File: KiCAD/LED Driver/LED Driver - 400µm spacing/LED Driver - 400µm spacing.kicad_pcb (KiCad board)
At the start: 2 copper layers, 13.1 x 9 mm, 6 parts, among them J1 0525590870, U1 LP5868TRKPR

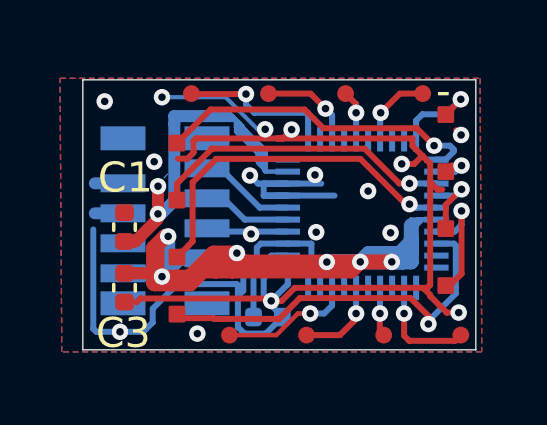
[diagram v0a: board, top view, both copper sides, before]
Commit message: Add controller - move ground
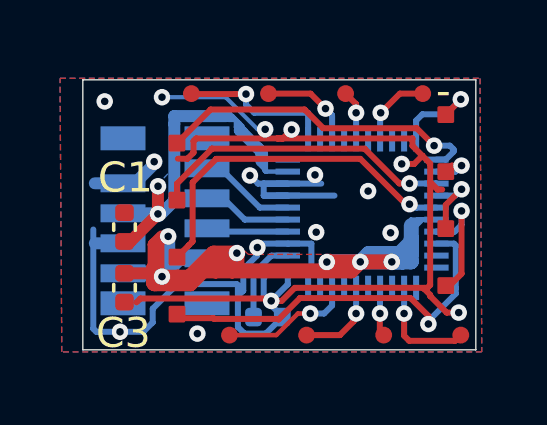
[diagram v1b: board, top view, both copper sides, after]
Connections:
- J1 pad 4: GND -> +5V
- J1 pad 6: +5V -> GND
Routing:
- net /VLED: track 41.4 -> 38.4 mm
- net GND: track 61.6 -> 62.8 mm, vias 17 -> 16
- net +5V: track 18.4 -> 17.5 mm
- added copper zone on F.Cu, net /VLED
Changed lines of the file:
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@@
 	(net 36 "unconnected-(U1-CS3-Pad4)")
 	(net 37 "unconnected-(U1-CS7-Pad8)")
+	(net 38 "unconnected-(J1-Pin_9-Pad9)")
+	(net 39 "unconnected-(J1-Pin_9-Pad9)_1")
+	(net 40 "unconnected-(J1-Pin_9-Pad9)_3")
 	(footprint "Capacitor_SMD:C_0402_1005Metric"
 		(layer "F.Cu")
@@
 			(size 0.6 1.5)
 			(layers "B.Cu" "B.Paste" "B.Mask")
-			(net 2 "GND")
+			(net 1 "+5V")
 			(pinfunction "Pin_4")
 			(pintype "passive")
@@
 			(size 0.6 1.5)
 			(layers "B.Cu" "B.Paste" "B.Mask")
-			(net 1 "+5V")
+			(net 2 "GND")
 			(pinfunction "Pin_6")
 			(pintype "passive")
@@
 			(size 0.8 1.5)
 			(layers "B.Cu" "B.Paste" "B.Mask")
-			(net 5 "unconnected-(J1-Pin_9-Pad9)_2")
+			(net 40 "unconnected-(J1-Pin_9-Pad9)_3")
 			(pinfunction "Pin_9")
 			(pintype "passive+no_connect")
@@
 			(size 0.8 1.5)
 			(layers "B.Cu" "B.Paste" "B.Mask")
-			(net 5 "unconnected-(J1-Pin_9-Pad9)_2")
+			(net 38 "unconnected-(J1-Pin_9-Pad9)")
 			(pinfunction "Pin_9")
 			(pintype "passive+no_connect")
@@
 			(size 0.8 1.5)
 			(layers "B.Cu" "B.Paste" "B.Mask")
-			(net 5 "unconnected-(J1-Pin_9-Pad9)_2")
+			(net 39 "unconnected-(J1-Pin_9-Pad9)_1")
 			(pinfunction "Pin_9")
 			(pintype "passive+no_connect")
@@
 	)
 	(segment
-		(start 47.88 35.09)
+		(start 47.715002 35.09)
 		(end 47.52 35.09)
 		(width 0.4)
@@
 	)
 	(segment
-		(start 48.635002 34.334998)
-		(end 47.88 35.09)
+		(start 48.635002 34.17)
+		(end 47.715002 35.09)
 		(width 0.4)
 		(layer "F.Cu")
@@
 	)
 	(segment
-		(start 48.655002 34.415002)
-		(end 49.28 33.790004)
-		(width 0.15)
+		(start 47.47 34.150004)
+		(end 48.615006 34.150004)
+		(width 0.4)
 		(layer "B.Cu")
 		(net 1)
@@
 	)
 	(segment
-		(start 47.92 35.150004)
-		(end 48.655002 34.415002)
-		(width 0.15)
-		(layer "B.Cu")
-		(net 1)
-	)
-	(segment
 		(start 51.370258 31.38)
 		(end 51.33 31.38)
@@
 	)
 	(segment
-		(start 48.655002 34.415002)
-		(end 48.635002 34.395002)
-		(width 0.15)
-		(layer "B.Cu")
-		(net 1)
-	)
-	(segment
-		(start 48.635002 34.395002)
-		(end 48.635002 34.17)
-		(width 0.15)
-		(layer "B.Cu")
-		(net 1)
-	)
-	(segment
-		(start 47.47 35.150004)
-		(end 47.92 35.150004)
-		(width 0.15)
-		(layer "B.Cu")
-		(net 1)
-	)
-	(segment
 		(start 51.98 31.989742)
 		(end 52.08 32.089742)
@@
 	)
 	(segment
+		(start 47.02 34.150004)
+		(end 47.47 34.150004)
+		(width 0.2)
+		(layer "B.Cu")
+		(net 1)
+	)
+	(segment
 		(start 52.19 32.687035)
 		(end 51.986482 32.483517)
@@
 	)
 	(segment
+		(start 48.615006 34.150004)
+		(end 48.635002 34.17)
+		(width 0.4)
+		(layer "B.Cu")
+		(net 1)
+	)
+	(segment
 		(start 49.905832 31.655)
 		(end 52.62 31.655)
@@
 		(net 2)
 	)
-	(segment
-		(start 58.74 31.54)
-		(end 58.58 31.38)
-		(width 0.2)
-		(layer "F.Cu")
-		(net 2)
-	)
 	(via
 		(at 51.7 32.89)
@@
 	)
 	(via
-		(at 51.74 34.84)
+		(at 51.95 35.29)
 		(size 0.55)
 		(drill 0.25)
@@
 	)
 	(via
-		(at 58.74 31.54)
-		(size 0.55)
-		(drill 0.25)
-		(layers "F.Cu" "B.Cu")
-		(free yes)
-		(net 2)
-	)
-	(via
 		(at 53.91 34.78)
 		(size 0.55)
@@
 	)
 	(segment
+		(start 47.47 35.150004)
+		(end 47.92 35.150004)
+		(width 0.15)
+		(layer "B.Cu")
+		(net 2)
+	)
+	(segment
 		(start 53.749999 35.959999)
 		(end 52.9635 35.959999)
@@
 	)
 	(segment
+		(start 48.51 32.43)
+		(end 48.51 32.50511)
+		(width 0.4)
+		(layer "B.Cu")
+		(net 2)
+	)
+	(segment
 		(start 52.497933 35.959999)
 		(end 52.16 36.297932)
@@
 	)
 	(segment
+		(start 47.47 35.150004)
+		(end 46.53 35.150004)
+		(width 0.4)
+		(layer "B.Cu")
+		(net 2)
+	)
+	(segment
 		(start 52.23 38.16)
 		(end 52.78 37.61)
@@
 	)
 	(segment
+		(start 48.51 32.50511)
+		(end 47.865106 33.150004)
+		(width 0.4)
+		(layer "B.Cu")
+		(net 2)
+	)
+	(segment
 		(start 49.28 36.509995)
 		(end 48.46 37.329995)
@@
 	)
 	(segment
+		(start 47.865106 33.150004)
+		(end 47.47 33.150004)
+		(width 0.4)
+		(layer "B.Cu")
+		(net 2)
+	)
+	(segment
 		(start 53.749999 35.160001)
 		(end 53.749999 35.959999)
@@
 	)
 	(segment
-		(start 47.47 34.150004)
-		(end 46.530004 34.150004)
-		(width 0.4)
-		(layer "B.Cu")
-		(net 2)
-	)
-	(segment
 		(start 51.299996 37.941278)
 		(end 51.299996 36.91)
@@
 	)
 	(segment
-		(start 47.02 34.150004)
-		(end 47.47 34.150004)
-		(width 0.2)
-		(layer "B.Cu")
-		(net 2)
-	)
-	(segment
 		(start 50.89 30.28)
 		(end 48.77 30.28)
@@
 	)
 	(segment
+		(start 48.76058 34.91942)
+		(end 48.49 35.19)
+		(width 0.4)
+		(layer "F.Cu")
+		(net 4)
+	)
+	(segment
 		(start 48.49 35.98)
 		(end 48.77 36.26)
@@
 	)
 	(segment
-		(start 48.878326 34.91942)
-		(end 48.49 35.307746)
-		(width 0.5)
-		(layer "F.Cu")
-		(net 4)
-	)
-	(segment
-		(start 51.454773 35.755227)
-		(end 51.265768 35.566221)
-		(width 0.5)
-		(layer "F.Cu")
-		(net 4)
-	)
-	(segment
-		(start 54.264999 35.775127)
-		(end 51.474673 35.775127)
-		(width 0.5)
-		(layer "F.Cu")
-		(net 4)
-	)
-	(segment
-		(start 48.976031 34.91942)
-		(end 48.878326 34.91942)
-		(width 0.5)
-		(layer "F.Cu")
-		(net 4)
-	)
-	(segment
-		(start 51.474673 35.775127)
-		(end 51.454773 35.755227)
-		(width 0.5)
-		(layer "F.Cu")
-		(net 4)
-	)
-	(segment
 		(start 49.73 36.55)
 		(end 50.21 36.07)
@@
 	)
 	(segment
-		(start 48.49 35.307746)
-		(end 48.49 35.98)
-		(width 0.5)
-		(layer "F.Cu")
-		(net 4)
-	)
-	(segment
 		(start 47.52 36.15)
 		(end 48.66 36.15)
@@
 	)
 	(segment
+		(start 48.49 35.19)
+		(end 48.49 35.98)
+		(width 0.4)
+		(layer "F.Cu")
+		(net 4)
+	)
+	(segment
 		(start 49.3 36.28)
 		(end 48.79 36.28)
@@
 		(net 4)
 	)
+	(segment
+		(start 48.976031 34.91942)
+		(end 48.76058 34.91942)
+		(width 0.2)
+		(layer "F.Cu")
+		(net 4)
+	)
 	(via
 		(at 56.43 35.77)
@@
 	)
 	(zone
+		(net 4)
+		(net_name "/VLED")
+		(layer "F.Cu")
+		(hatch edge 0.5)
+		(priority 2)
+		(connect_pads yes
+			(clearance 0.15)
+		)
+		(min_thickness 0.25)
+		(filled_areas_thickness no)
+		(fill yes
+			(thermal_gap 0.5)
+			(thermal_bridge_width 0.5)
+		)
+		(polygon
+			(pts
+				(xy 54.41 35.52) (xy 51.65 35.52) (xy 51.31 35.21) (xy 51.02 35.52) (xy 51 36.02) (xy 52.04 36.2)
+				(xy 54.4 36.25)
+			)
+		)
+	)
+	(zone

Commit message: Add microcontroller
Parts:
- removed HS1: Heatsink, Custom:heatsink
- removed J1: 0525590870, Custom:CON_525590870_MOL - 8x ribbon vert
- added C4: 1µF, Capacitor_SMD:C_0402_1005Metric_Pad0.74x0.62mm_HandSolder, B.Cu at (47.1, 33.8)
- added D1: D_Photo, Custom:DIO_VEMD4110X01, B.Cu at (49.9, 30.7)
- added R1: 1M, Resistor_SMD:R_0402_1005Metric, B.Cu at (48.0, 31.2)
- added U2: ATtiny3226, Custom:ATtiny3226, B.Cu at (49.7, 34.0)
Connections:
- C3 pad 2: /VLED -> +5V
- U1 pad 16: /VLED -> +5V
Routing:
- net /VLED: track 38.4 -> 0.00 mm, vias 6 -> 0
- net +5V: track 17.5 -> 37.6 mm, vias 2 -> 10
- net GND: track 62.8 -> 48.9 mm, vias 16 -> 23
- net /Photodiode: track 0.00 -> 5.06 mm
- net /SDA: track 3.71 -> 1.88 mm
- net /SCL: track 2.99 -> 1.88 mm
- net /Col6: track 11.8 -> 10.8 mm
- net /Vsync: track 2.74 -> 1.88 mm
- net /Col4: track 10.2 -> 9.38 mm
- added copper zone on F.Cu, net +5V
- removed copper zone on F.Cu, net /VLED
